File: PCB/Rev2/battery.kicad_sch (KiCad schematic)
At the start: 16 parts, among them U4 LGS5500EP

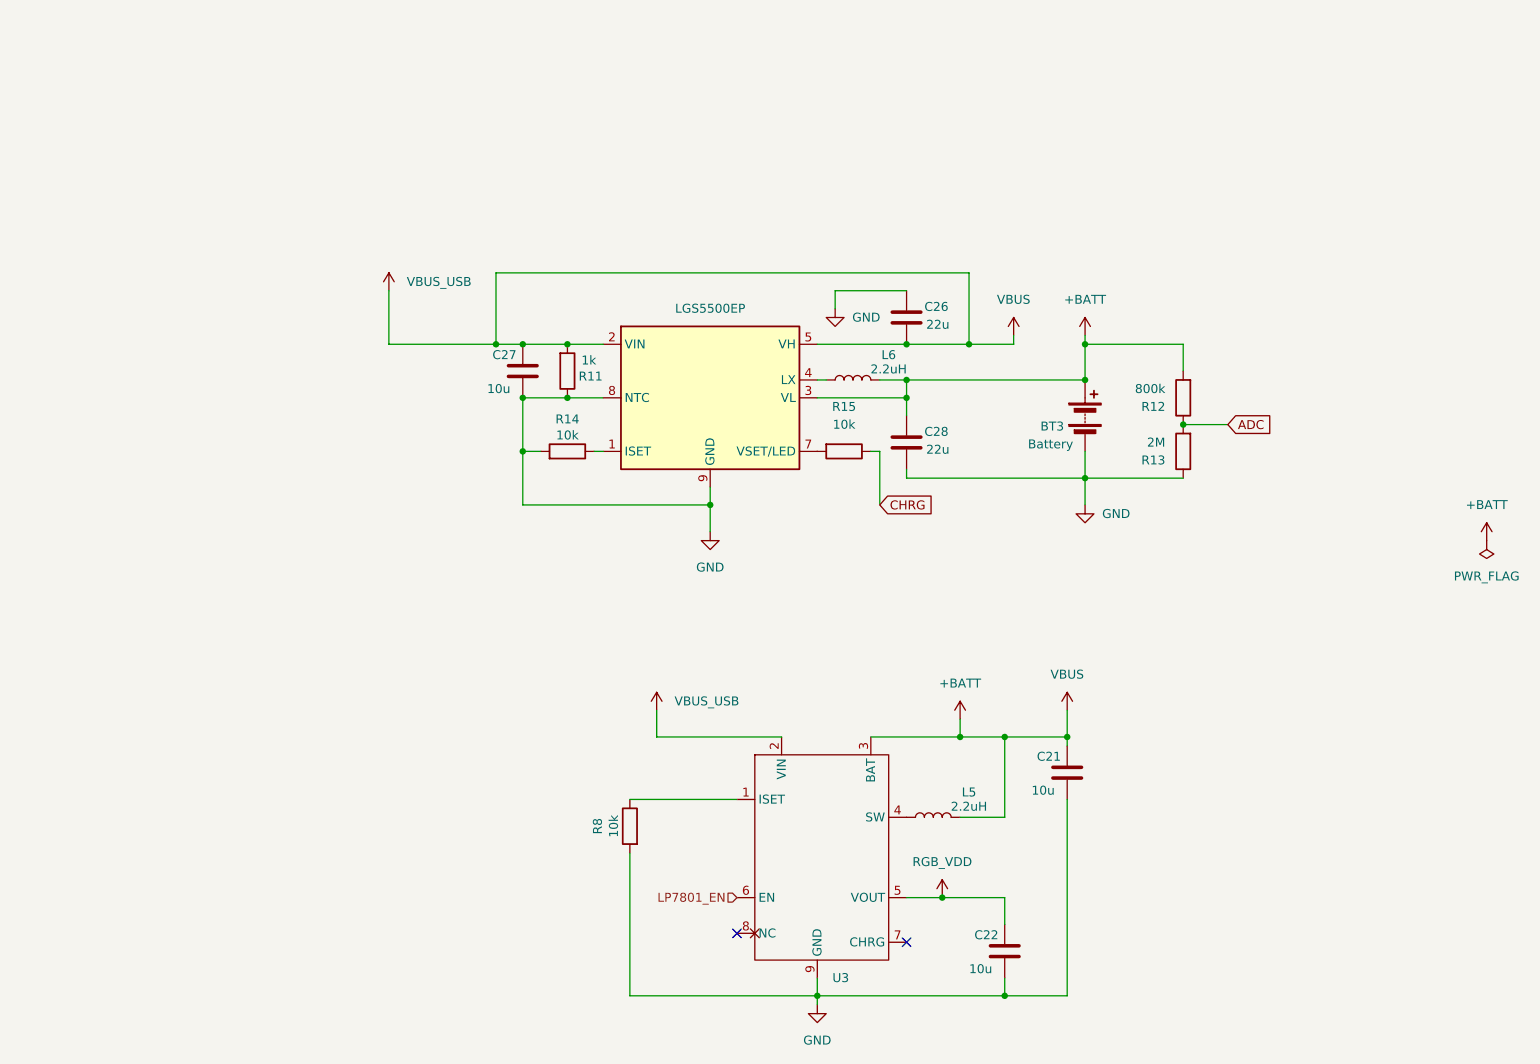
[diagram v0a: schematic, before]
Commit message: Update charger symbol and net
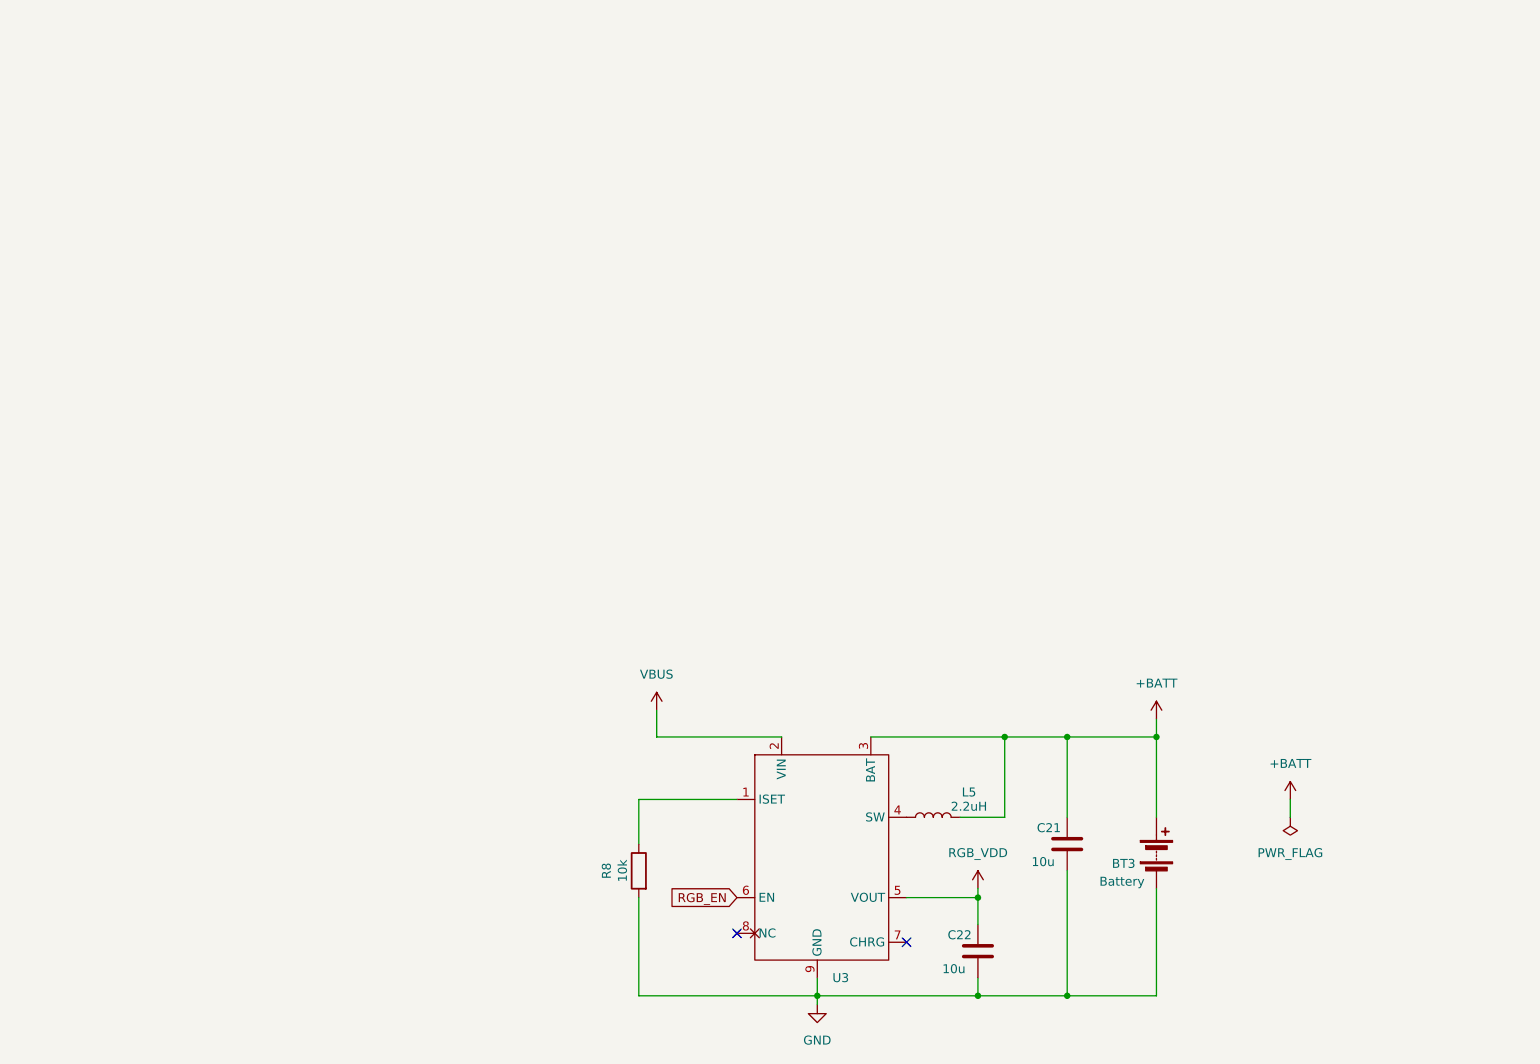
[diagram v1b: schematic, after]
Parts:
- removed C26, C28: 22u, Capacitor_SMD:C_0603_1608Metric, symbol Device:C
- removed C27: 10u, Capacitor_SMD:C_0402_1005Metric, symbol Device:C
- removed L6: 2.2uH, Inductor_SMD:L_Changjiang_FNR252012S, symbol Device:L
- removed R11: 1k, PCM_Resistor_SMD_AKL:R_0402_1005Metric, symbol Device:R
- removed R12: 800k, PCM_Resistor_SMD_AKL:R_0603_1608Metric, symbol Device:R
- removed R13: 2M, PCM_Resistor_SMD_AKL:R_0603_1608Metric, symbol Device:R
- removed R14, R15: 10k, PCM_Resistor_SMD_AKL:R_0402_1005Metric, symbol Device:R
- removed U4: LGS5500EP, Package_SO:SOIC-8-1EP_3.9x4.9mm_P1.27mm_EP2.41x3.3mm, symbol Battery_Management:LGS5500EP
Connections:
- net +BATT: no longer U3.2 (VIN)
- net LP7801_EN renamed RGB_EN
- new net VBUS: U3.2 (VIN)
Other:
- moved on the sheet: BT3, C21, C22, R8

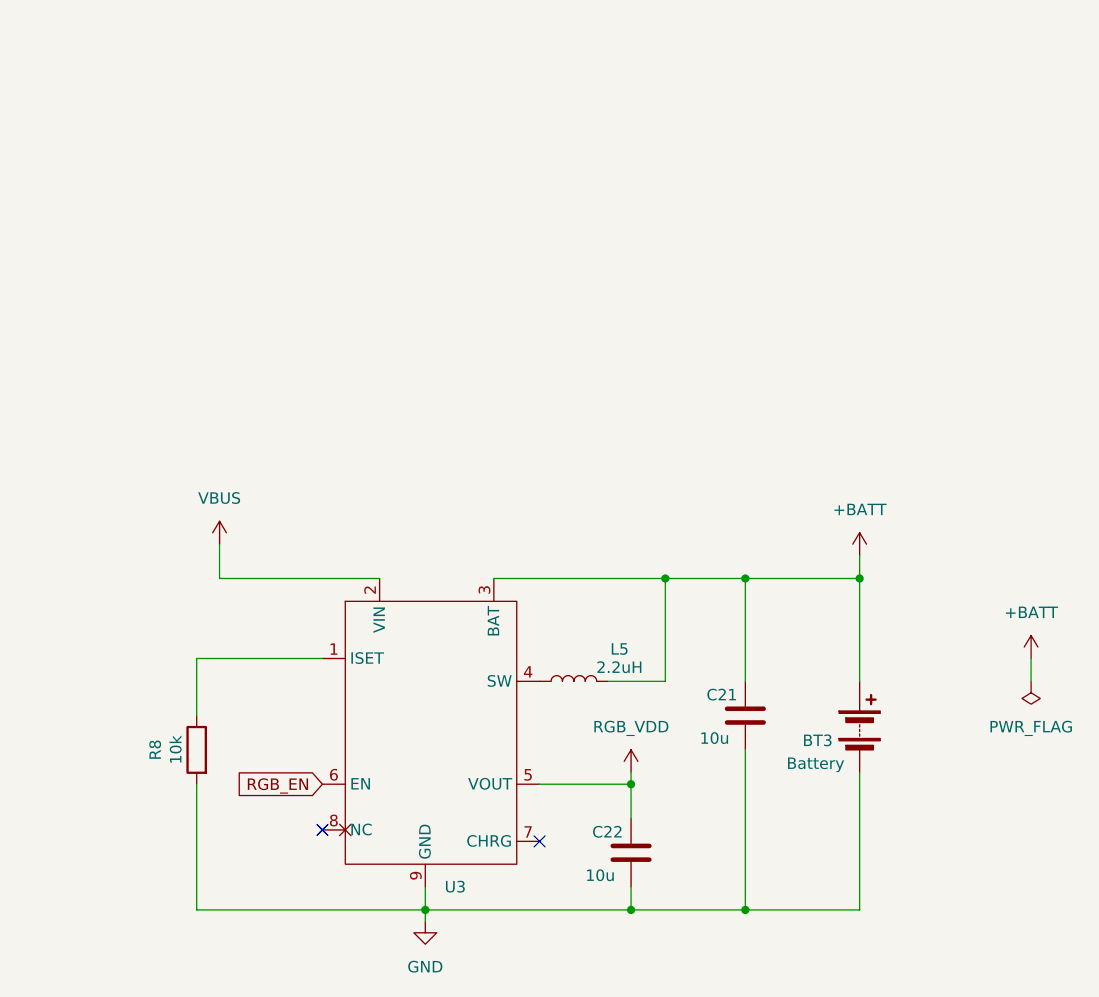
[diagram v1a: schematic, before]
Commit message: 锂电池充电设置电阻调整至3.4kΩ
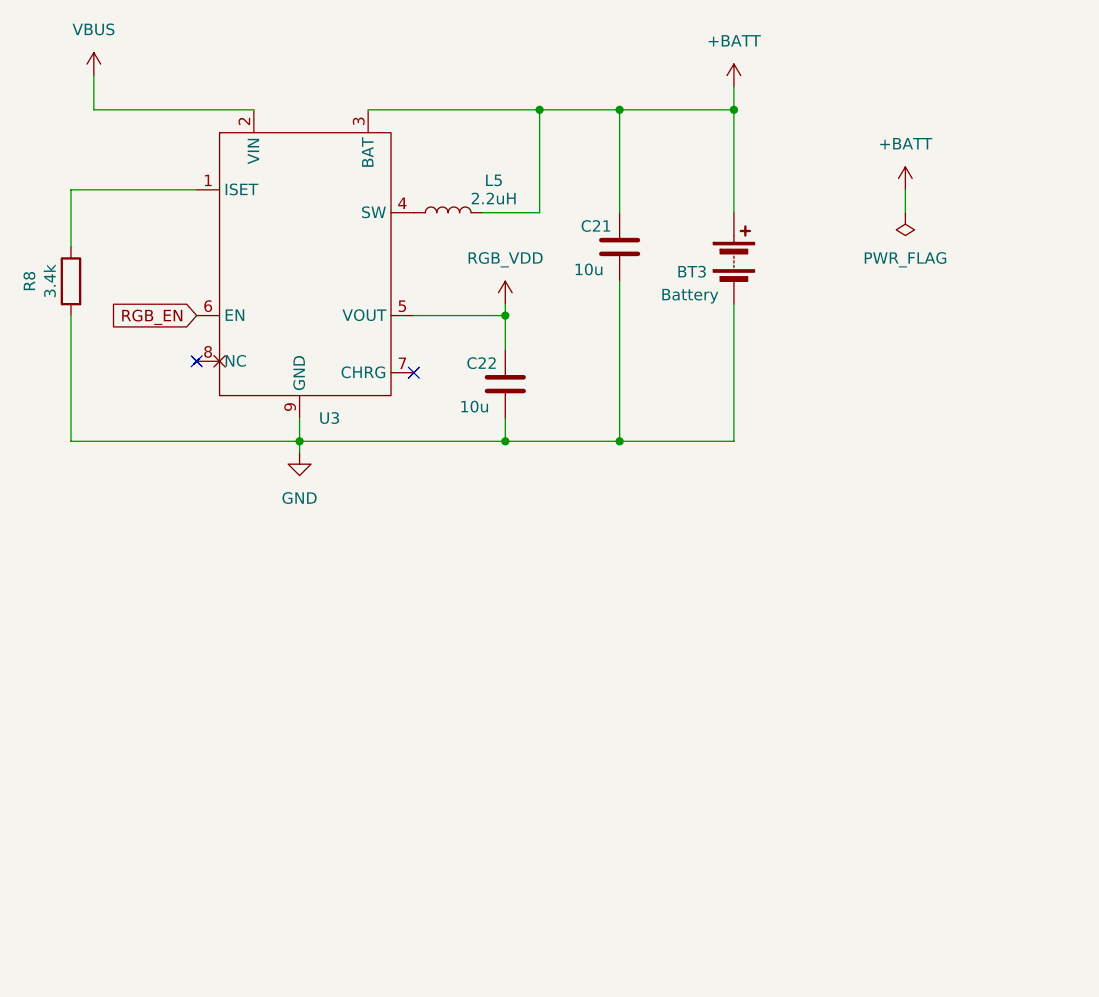
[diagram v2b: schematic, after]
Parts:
- R8: value 10k -> 3.4k
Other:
- moved on the sheet: BT3, C21, C22, L5, R8, U3

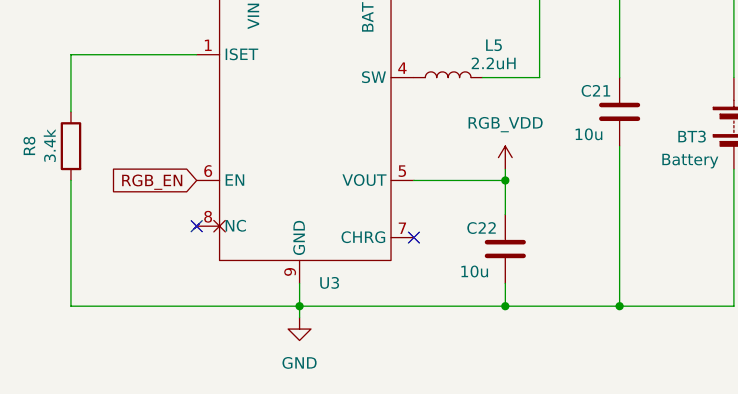
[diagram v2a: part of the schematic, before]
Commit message: 电源封装修改
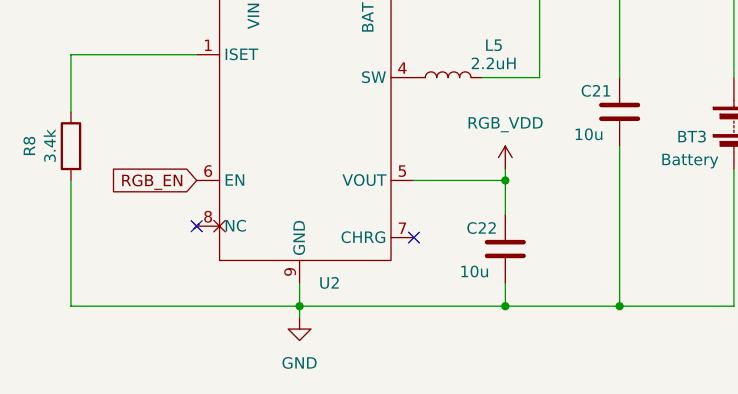
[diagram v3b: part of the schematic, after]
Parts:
- removed U3: ~, Package_SO:SOP-8-1EP_4.57x4.57mm_P1.27mm_EP4.57x4.45mm, symbol LP7801D_sym:LP7801D
- added U2: ~, Package_SO:SOIC-8-1EP_3.9x4.9mm_P1.27mm_EP2.41x3.3mm, symbol LP7801D_sym:LP7801D
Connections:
- net +BATT: now also U2.3 (BAT)
- net GND: now also U2.9 (GND)
- net RGB_EN: now also U2.6 (EN)
- net RGB_VDD: now also U2.5 (VOUT)
- net VBUS: now also U2.2 (VIN)
- net at R8.1: now also U2.1 (ISET)
- net at L5.1: now also U2.4 (SW)
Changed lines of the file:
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@@
+	)
+	(symbol
+		(lib_id "LP7801D_sym:LP7801D")
+		(at 97.79 59.69 0)
+		(unit 1)
+		(exclude_from_sim no)
+		(in_bom yes)
+		(on_board yes)
+		(dnp no)
+		(fields_autoplaced yes)
+		(property "Reference" "U2"
+			(at 115.1733 96.52 0)
+			(effects
+				(font
+					(size 1.27 1.27)
+				)
+				(justify left)
+			)
+		)
+		(property "Value" "~"
+			(at 115.1733 99.06 0)
+			(effects
+				(font
+					(size 1.27 1.27)
+				)
+				(justify left)
+			)
+		)
+		(property "Footprint" "Package_SO:SOIC-8-1EP_3.9x4.9mm_P1.27mm_EP2.41x3.3mm"
+			(at 109.474 104.648 0)
+			(effects
+				(font
+					(size 1.27 1.27)
+				)
+				(hide yes)
+			)
+		)
+		(property "Datasheet" ""
+			(at 97.79 59.69 0)
+			(effects
+				(font
+					(size 1.27 1.27)
+				)
+				(hide yes)
+			)
+		)
+		(property "Description" ""
+			(at 97.79 59.69 0)
+			(effects
+				(font
+					(size 1.27 1.27)
+				)
+				(hide yes)
+			)
+		)
+		(pin "9"
+		)
+		(pin "6"
+		)
+		(pin "1"
+		)
+		(pin "4"
+		)
+		(pin "2"
+		)
+		(pin "8"
+		)
+		(pin "3"
+		)
+		(pin "7"
+		)
+		(pin "5"
+		)
+		(instances
+			(project ""
+				(path "/dca0f898-8fdb-4522-a51d-f4f4238906e7/65afedf5-5b27-4d53-9ad9-9264a927261c"
+					(reference "U2")
+					(unit 1)
+				)
+			)
+		)
 	)
 	(symbol
@@
 					(unit 1)
 				)
-			)
-		)
-	)
-	(symbol
-		(lib_id "LP7801D_sym:LP7801D")
-		(at 97.79 59.69 0)
-		(unit 1)
-		(exclude_from_sim no)
-		(in_bom yes)
-		(on_board yes)
-		(dnp no)
-		(fields_autoplaced yes)
-		(property "Reference" "U3"
-			(at 115.1733 96.52 0)
-			(effects
-				(font
-					(size 1.27 1.27)
-				)
-				(justify left)
-			)
-		)
-		(property "Value" "~"
-			(at 115.1733 99.06 0)
-			(effects
-				(font
-					(size 1.27 1.27)
-				)
-				(justify left)
-				(hide yes)
-			)
-		)
-		(property "Footprint" "Package_SO:SOP-8-1EP_4.57x4.57mm_P1.27mm_EP4.57x4.45mm"
-			(at 109.474 104.648 0)
-			(effects
-				(font
-					(size 1.27 1.27)
-				)
-				(hide yes)
-			)
-		)
-		(property "Datasheet" ""
-			(at 97.79 59.69 0)
-			(effects
-				(font
-					(size 1.27 1.27)
-				)
-				(hide yes)
-			)
-		)
-		(property "Description" ""
-			(at 97.79 59.69 0)
-			(effects
-				(font
-					(size 1.27 1.27)
-				)
-				(hide yes)
-			)
-		)
-		(pin "1"
-		)
-		(pin "4"
-		)
-		(pin "7"
-		)
-		(pin "2"
-		)
-		(pin "6"
-		)
-		(pin "9"
-		)
-		(pin "5"
-		)
-		(pin "3"
-		)
-		(pin "8"
-		)
-		(instances
-			(project ""
-				(path "/dca0f898-8fdb-4522-a51d-f4f4238906e7/65afedf5-5b27-4d53-9ad9-9264a927261c"
-					(reference "U3")
-					(unit 1)
-				)

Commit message: 电源芯片设计
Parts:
- removed BT3: Battery, Connector_Molex:Molex_Panelmate_53780-0270_1x02-1MP_P1.25mm_Horizontal, symbol Device:Battery
- removed C21, C22: 10u, Capacitor_SMD:C_0402_1005Metric, symbol Device:C
- removed L5: 2.2uH, Inductor_SMD:L_Changjiang_FNR252012S, symbol Device:L
- removed R8: 3.4k, PCM_Resistor_SMD_AKL:R_0402_1005Metric, symbol Device:R
- removed U2: ~, Package_SO:SOIC-8-1EP_3.9x4.9mm_P1.27mm_EP2.41x3.3mm, symbol LP7801D_sym:LP7801D
- added BT2: Battery, Connector_Molex:Molex_PicoBlade_53261-0271_1x02-1MP_P1.25mm_Horizontal, symbol Device:Battery
- added C26, C29: 2.2u, Capacitor_SMD:C_0402_1005Metric, symbol Device:C
- added C27: 4.7u, Capacitor_SMD:C_0402_1005Metric, symbol Device:C
- added C28: 1u, Capacitor_SMD:C_0402_1005Metric, symbol Device:C
- added R10, R6: 330k, Resistor_SMD:R_0402_1005Metric, symbol Device:R
- added R11, R7: 100k, Resistor_SMD:R_0402_1005Metric, symbol Device:R
- added R12: 2k, Resistor_SMD:R_0402_1005Metric, symbol Device:R
- added U3: TP4057, Package_TO_SOT_SMD:TSOT-23-6, symbol Battery_Management:TP4057
- added U4, U5: TPS2116DRL, Package_TO_SOT_SMD:SOT-583-8, symbol Power_Management:TPS2116DRL
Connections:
- net +BATT: now also BT2.1 (+), C28.1, U3.3 (BAT), U4.6 (VIN2), U5.6 (VIN2)
- net GND: now also BT2.2 (-), C26.2, C27.2, C28.2, C29.2, R11.2, R12.2, R7.2, U3.2 (GND), U4.1 (GND), U5.1 (GND)
- net RGB_VDD: now also C29.1, U5.2 (VOUT), U5.7 (VOUT)
- net VBUS: now also C27.1, R10.1, R6.1, U3.4 (V_{CC}), U4.3 (VIN1), U4.5 (MODE), U5.3 (VIN1), U5.5 (MODE)
- new net: R10.2, R11.1, U4.4 (PR1)
- new net: R6.2, R7.1, U5.4 (PR1)
- new net: R12.1, U3.6 (PROG)
- new net BATT_STAT: U4.8 (ST), U5.8 (ST)
- new net VDD: C26.1, U4.2 (VOUT), U4.7 (VOUT)
